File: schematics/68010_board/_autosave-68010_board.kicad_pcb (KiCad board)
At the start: 2 copper layers, 124.5 x 73.5 mm, 7 parts, among them IC1 MC68010R, J2 80-bit bus, SW1 CLK DIP Switch, SW2 Reset, U1 SN74HC4040N, U2 DS1813-5, X1 Crystal Oscillator

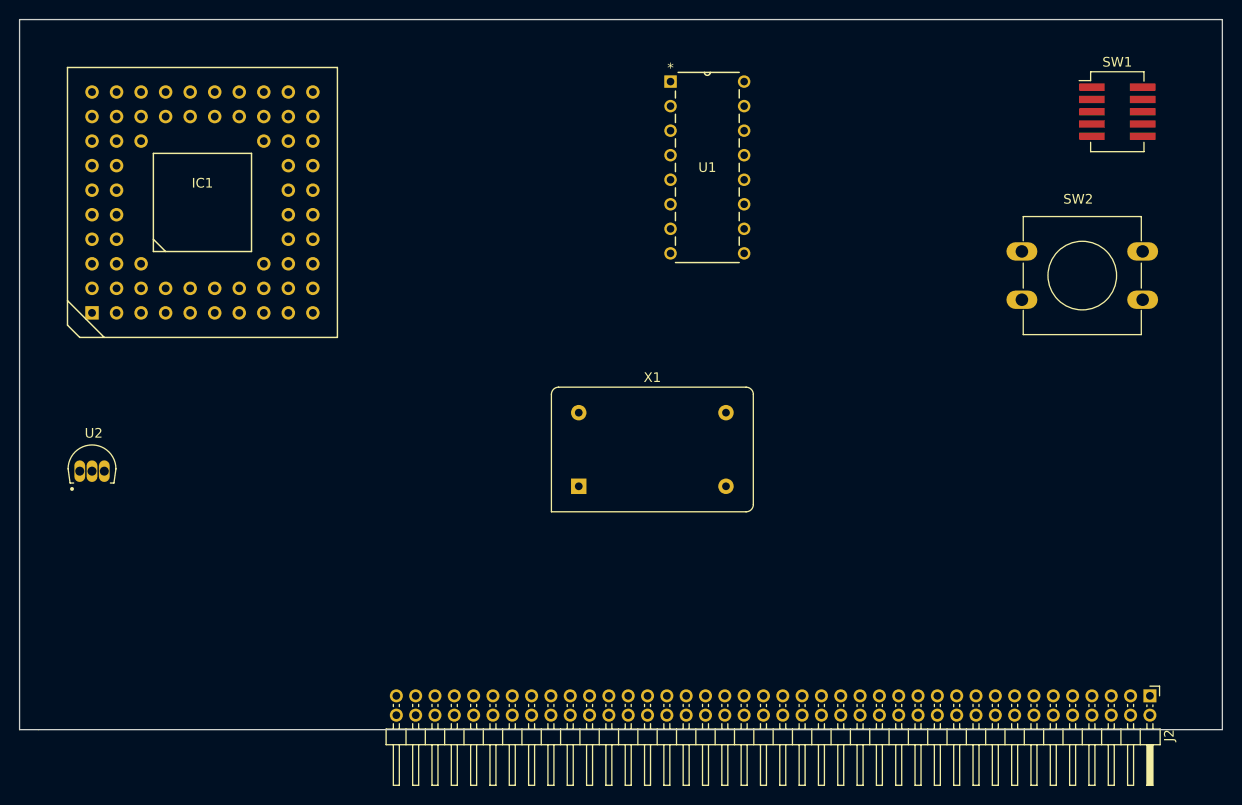
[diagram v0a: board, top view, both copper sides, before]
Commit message: aether: Add updated schematics (64->80 pin header, future-proofing)
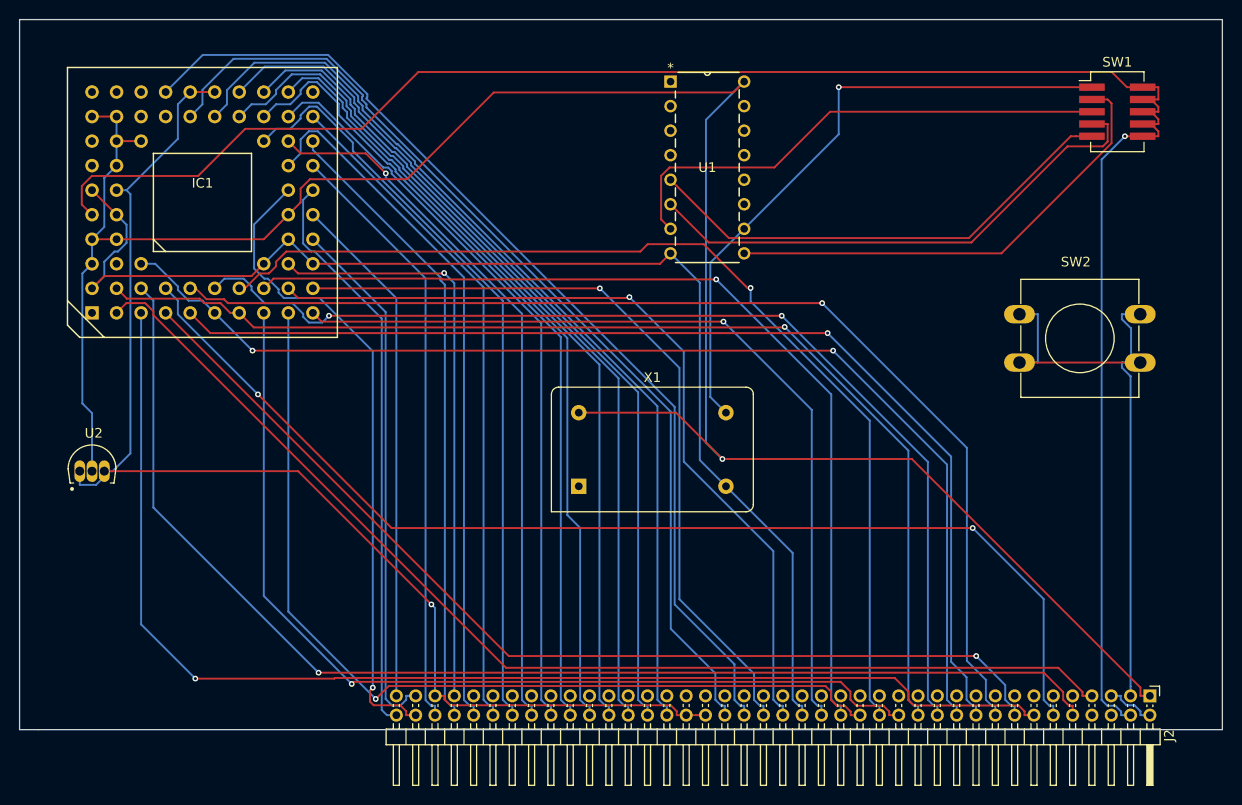
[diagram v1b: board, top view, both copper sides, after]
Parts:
- moved SW2 6.50 mm to (153.5, 80.5)
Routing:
- net +5V: track 0.00 -> 231.9 mm, vias 0 -> 1
- net /CLK: track 0.00 -> 198.1 mm, vias 0 -> 1
- net /RESET: track 0.00 -> 196.2 mm, vias 0 -> 1
- net GND: track 0.00 -> 135.7 mm
- net Net-(IC1A-D1): track 0.00 -> 129.4 mm, vias 0 -> 1
- net /UDS: track 0.00 -> 128.3 mm, vias 0 -> 1
- net /R/W: track 0.00 -> 118.8 mm, vias 0 -> 2
- net /AS: track 0.00 -> 118.7 mm
- net /D0: track 0.00 -> 117.7 mm, vias 0 -> 2
- net /LDS: track 0.00 -> 117.0 mm, vias 0 -> 1
- net Net-(IC1A-D3): track 0.00 -> 116.3 mm, vias 0 -> 1
- net Net-(IC1A-D4): track 0.00 -> 113.0 mm, vias 0 -> 1
- net Net-(IC1A-D6): track 0.00 -> 109.9 mm, vias 0 -> 2
- net Net-(IC1A-D9): track 0.00 -> 107.0 mm, vias 0 -> 1
- net Net-(IC1A-D2): track 0.00 -> 106.6 mm, vias 0 -> 1
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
